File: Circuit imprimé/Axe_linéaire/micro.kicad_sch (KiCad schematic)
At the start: 6 parts, among them Q1 LP2301LT1G, SW1 SW_MEC_5G, U1 PicoW

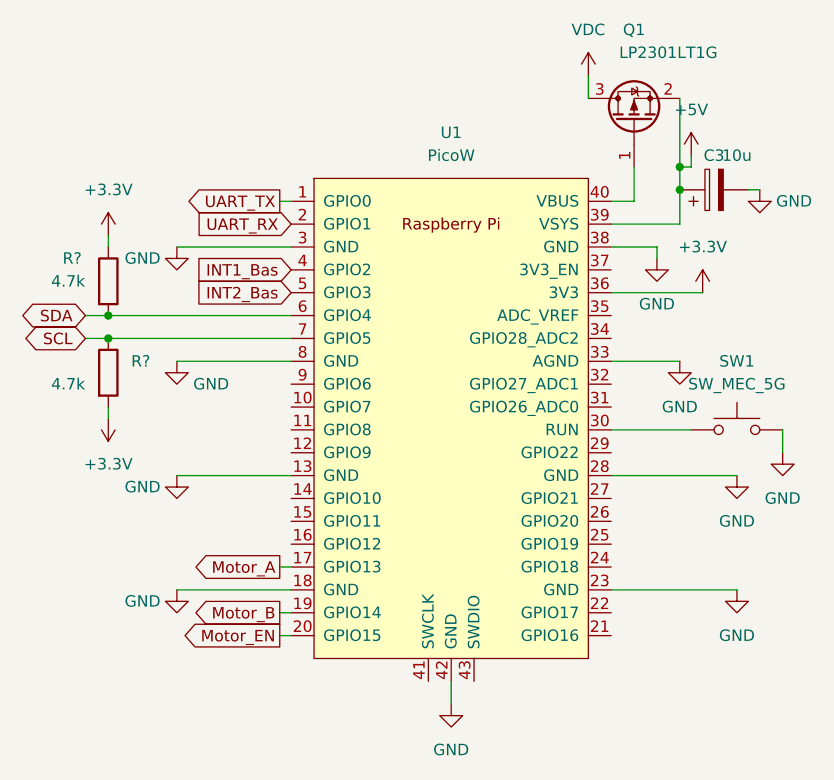
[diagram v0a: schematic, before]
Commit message: ajout du circuit de position + carte SD
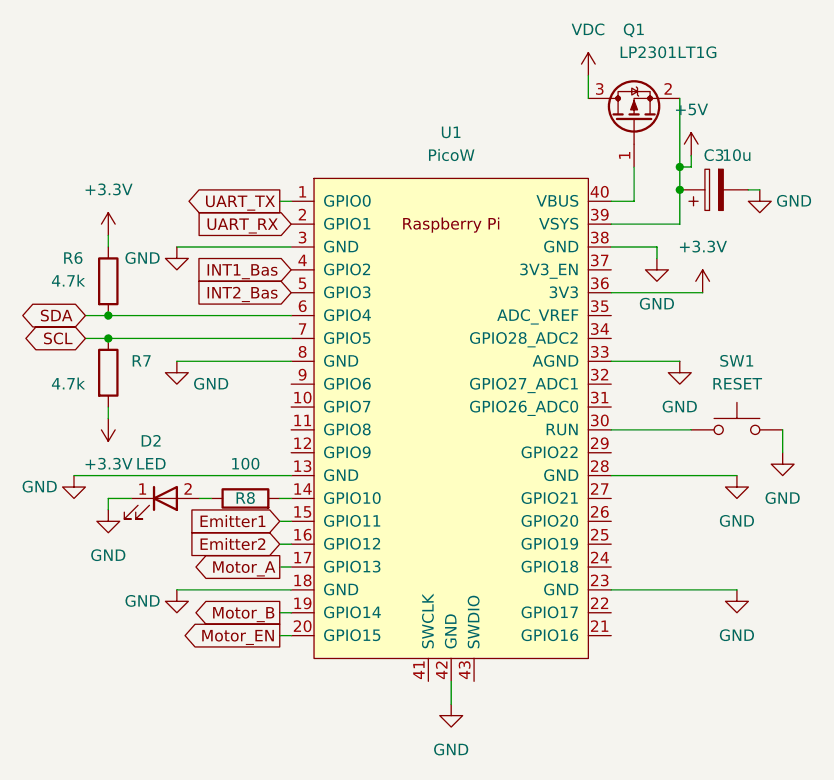
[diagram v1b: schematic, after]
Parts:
- added D2: LED, Library:UV_LED, symbol Device:LED
- added R8: 100, symbol Device:R
- SW1: value SW_MEC_5G -> RESET
- gave numbers to parts that had none: 2
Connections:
- net GND: now also D2.1 (K)
- net at U1.14 (GPIO10): now also R8.2
- net Emitter1: now reaches U1.15 (GPIO11)
- net Emitter2: now reaches U1.16 (GPIO12)
- new net: D2.2 (A), R8.1
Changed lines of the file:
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@@
+    (stroke (width 0) (type default) (color 0 0 0 0))
+  )
+  (wire (pts (xy 121.92 80.01) (xy 123.19 80.01))
     (stroke (width 0) (type default) (color 0 0 0 0))
   )
@@
     (stroke (width 0) (type default) (color 0 0 0 0))
   )
+  (wire (pts (xy 102.87 77.47) (xy 105.41 77.47))
+    (stroke (width 0) (type default) (color 0 0 0 0))
+  )
   (wire (pts (xy 166.37 46.99) (xy 166.37 43.18))
     (stroke (width 0) (type default) (color 0 0 0 0))
@@
     (stroke (width 0) (type default) (color 0 0 0 0))
   )
+  (wire (pts (xy 113.03 77.47) (xy 114.3 77.47))
+    (stroke (width 0) (type default) (color 0 0 0 0))
+  )
+  (wire (pts (xy 121.92 77.47) (xy 123.19 77.47))
+    (stroke (width 0) (type default) (color 0 0 0 0))
+  )
+  (wire (pts (xy 121.92 82.55) (xy 123.19 82.55))
+    (stroke (width 0) (type default) (color 0 0 0 0))
+  )
   (wire (pts (xy 102.87 48.26) (xy 102.87 49.53))
     (stroke (width 0) (type default) (color 0 0 0 0))
   )
+  (wire (pts (xy 102.87 77.47) (xy 102.87 78.74))
+    (stroke (width 0) (type default) (color 0 0 0 0))
+  )
   (wire (pts (xy 121.92 44.45) (xy 123.19 44.45))
     (stroke (width 0) (type default) (color 0 0 0 0))
@@
     (stroke (width 0) (type default) (color 0 0 0 0))
   )
-  (wire (pts (xy 110.49 74.93) (xy 123.19 74.93))
+  (wire (pts (xy 99.06 74.93) (xy 123.19 74.93))
     (stroke (width 0) (type default) (color 0 0 0 0))
   )
@@
     )
   )
+  (global_label "Emitter1" (shape input) (at 121.92 80.01 180) (fields_autoplaced)
+    (effects (font (size 1.27 1.27)) (justify right))
+    (property "Intersheet References" "${INTERSHEET_REFS}" (id 0) (at 111.524 79.9306 0)
+      (effects (font (size 1.27 1.27)) (justify right) hide)
+    )
+  )
   (global_label "INT2_Bas" (shape input) (at 123.19 54.61 180) (fields_autoplaced)
     (effects (font (size 1.27 1.27)) (justify right))
@@
     )
   )
+  (global_label "Emitter2" (shape input) (at 121.92 82.55 180) (fields_autoplaced)
+    (effects (font (size 1.27 1.27)) (justify right))
+    (property "Intersheet References" "${INTERSHEET_REFS}" (id 0) (at 111.524 82.4706 0)
+      (effects (font (size 1.27 1.27)) (justify right) hide)
+    )
+  )
   (global_label "Motor_EN" (shape output) (at 121.92 92.71 180) (fields_autoplaced)
     (effects (font (size 1.27 1.27)) (justify right))
@@
     )
   )
+  (symbol (lib_id "power:GND") (at 102.87 78.74 0) (unit 1)
+    (in_bom yes) (on_board yes) (fields_autoplaced)
+    (property "Reference" "#PWR038" (id 0) (at 102.87 85.09 0)
+      (effects (font (size 1.27 1.27)) hide)
+    )
+    (property "Value" "GND" (id 1) (at 102.87 83.82 0))
+    (property "Footprint" "" (id 2) (at 102.87 78.74 0)
+      (effects (font (size 1.27 1.27)) hide)
+    )
+    (property "Datasheet" "" (id 3) (at 102.87 78.74 0)
+      (effects (font (size 1.27 1.27)) hide)
+    )
+    (pin "1")
+  )
   (symbol (lib_id "power:+5V") (at 167.64 39.37 0) (unit 1)
     (in_bom yes) (on_board yes) (fields_autoplaced)
@@
     (pin "1")
   )
+  (symbol (lib_id "Device:R") (at 118.11 77.47 90) (unit 1)
+    (in_bom yes) (on_board yes)
+    (property "Reference" "R8" (id 0) (at 118.11 77.47 90))
+    (property "Value" "100" (id 1) (at 118.11 73.66 90))
+    (property "Footprint" "" (id 2) (at 118.11 79.248 90)
+      (effects (font (size 1.27 1.27)) hide)
+    )
+    (property "Datasheet" "~" (id 3) (at 118.11 77.47 0)
+      (effects (font (size 1.27 1.27)) hide)
+    )
+    (pin "1")
+    (pin "2")
+  )
   (symbol (lib_id "power:+3.3V") (at 102.87 68.58 180) (unit 1)
     (in_bom yes) (on_board yes) (fields_autoplaced)
-    (property "Reference" "#PWR?" (id 0) (at 102.87 64.77 0)
+    (property "Reference" "#PWR037" (id 0) (at 102.87 64.77 0)
       (effects (font (size 1.27 1.27)) hide)
     )
@@
   (symbol (lib_id "Device:R") (at 102.87 63.5 0) (unit 1)
     (in_bom yes) (on_board yes)
-    (property "Reference" "R?" (id 0) (at 105.41 62.2299 0)
+    (property "Reference" "R7" (id 0) (at 105.41 62.2299 0)
       (effects (font (size 1.27 1.27)) (justify left))
     )
@@
     )
     (property "Datasheet" "~" (id 3) (at 102.87 63.5 0)
+      (effects (font (size 1.27 1.27)) hide)
+    )
+    (pin "1")
+    (pin "2")
+  )
+  (symbol (lib_id "Device:LED") (at 109.22 77.47 0) (unit 1)
+    (in_bom yes) (on_board yes) (fields_autoplaced)
+    (property "Reference" "D2" (id 0) (at 107.6325 71.12 0))
+    (property "Value" "LED" (id 1) (at 107.6325 73.66 0))
+    (property "Footprint" "Library:UV_LED" (id 2) (at 109.22 77.47 0)
+      (effects (font (size 1.27 1.27)) hide)
+    )
+    (property "Datasheet" "~" (id 3) (at 109.22 77.47 0)
       (effects (font (size 1.27 1.27)) hide)
     )
@@
   (symbol (lib_id "power:+3.3V") (at 102.87 48.26 0) (unit 1)
     (in_bom yes) (on_board yes) (fields_autoplaced)
-    (property "Reference" "#PWR?" (id 0) (at 102.87 52.07 0)
+    (property "Reference" "#PWR036" (id 0) (at 102.87 52.07 0)
       (effects (font (size 1.27 1.27)) hide)
     )
@@
     (pin "1")
   )
-  (symbol (lib_id "power:GND") (at 110.49 74.93 0) (unit 1)
+  (symbol (lib_id "power:GND") (at 99.06 74.93 0) (unit 1)
     (in_bom yes) (on_board yes)
-    (property "Reference" "#PWR03" (id 0) (at 110.49 81.28 0)
-      (effects (font (size 1.27 1.27)) hide)
-    )
-    (property "Value" "GND" (id 1) (at 106.68 76.2 0))
-    (property "Footprint" "" (id 2) (at 110.49 74.93 0)
-      (effects (font (size 1.27 1.27)) hide)
-    )
-    (property "Datasheet" "" (id 3) (at 110.49 74.93 0)
+    (property "Reference" "#PWR03" (id 0) (at 99.06 81.28 0)
+      (effects (font (size 1.27 1.27)) hide)
+    )
+    (property "Value" "GND" (id 1) (at 95.25 76.2 0))
+    (property "Footprint" "" (id 2) (at 99.06 74.93 0)
+      (effects (font (size 1.27 1.27)) hide)
+    )
+    (property "Datasheet" "" (id 3) (at 99.06 74.93 0)
       (effects (font (size 1.27 1.27)) hide)
     )
@@
   (symbol (lib_id "Device:R") (at 102.87 53.34 0) (unit 1)
     (in_bom yes) (on_board yes)
-    (property "Reference" "R?" (id 0) (at 97.79 50.8 0)
+    (property "Reference" "R6" (id 0) (at 97.79 50.8 0)
       (effects (font (size 1.27 1.27)) (justify left))
     )
@@
     (in_bom yes) (on_board yes) (fields_autoplaced)
     (property "Reference" "SW1" (id 0) (at 172.72 62.23 0))
-    (property "Value" "SW_MEC_5G" (id 1) (at 172.72 64.77 0))
+    (property "Value" "RESET" (id 1) (at 172.72 64.77 0))
     (property "Footprint" "Library:Tactile Button" (id 2) (at 172.72 64.77 0)
       (effects (font (size 1.27 1.27)) hide)
